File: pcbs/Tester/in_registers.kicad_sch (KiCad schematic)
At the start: 11 parts, among them U401 74HC165, U402 74HC165, U403 74HC165

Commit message: Lots of rethinking
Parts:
- added J401: Conn_02x20_Odd_Even, Connector_PinHeader_2.54mm:PinHeader_2x20_P2.54mm_Vertical, symbol Connector_Generic:Conn_02x20_Odd_Even
- added R409, R410, R411, R412, R413, R414, R415, R416, R417, R418, R419, R420, R421, R422, R423, R424, R425, R426, R427, R428, R429, R430, R431, R432, R433, R434, R435, R436, R437, R438, R439, R440: 1M, Resistor_SMD:R_0603_1608Metric, symbol Device:R
- added U403, U404: 74HC165, Package_SO:SOIC-16_3.9x9.9mm_P1.27mm, symbol 74xx:74HC165
- renumbered U403 to U405
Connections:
- net +5V: now also U403.16 (VCC), U404.16 (VCC)
- net GND: now also U405.10 (DS), R409.2, R410.2, R411.2, R412.2, R413.2, R414.2, R415.2, R416.2, R417.2, R418.2, R419.2, R420.2, R421.2, R422.2, R423.2, R424.2, R425.2, R426.2, R427.2, R428.2, R429.2, R430.2, R431.2, R432.2, R433.2, R434.2, R435.2, R436.2, R437.2, R438.2, R439.2, R440.2, U403.8 (GND), U404.8 (GND); no longer U401.10 (DS)
- net IN_{CLK}: now also U403.2 (CP), U404.2 (CP)
- net IN_{DATA}: now also U401.9 (Q7); no longer U405.9 (Q7)
- net ~{IN_{LOAD}}: now also U403.1 (~{PL}), U404.1 (~{PL})
- net ~{IN_{SELECT}}: now also U403.15 (~{CE}), U404.15 (~{CE})
- net at U402.10 (DS): now also U403.9 (Q7); no longer U401.9 (Q7)
- net at U402.9 (Q7): now also U401.10 (DS); no longer U405.10 (DS)
- net IN0: no longer names the net of U405.6 (D7)
- net IN0: no longer R401.1
- net IN1: no longer names the net of U405.5 (D6)
- net IN1: no longer R402.1
- net IN16 renamed In_{0}
- net In_{0}: now also R401.1, J401.1 (Pin_1)
- net IN17 renamed In_{1}
- net In_{1}: now also R402.1, J401.2 (Pin_2)
- net IN18 renamed In_{2}
- net In_{2}: now also R403.1, J401.3 (Pin_3)
- net IN19 renamed In_{3}
- net In_{3}: now also R404.1, J401.4 (Pin_4)
- net IN2: no longer names the net of U405.4 (D5)
- net IN2: no longer R403.1
- net IN20 renamed In_{4}
- net In_{4}: now also R405.1, J401.5 (Pin_5)
- net IN21 renamed In_{5}
- net In_{5}: now also R406.1, J401.6 (Pin_6)
- net IN22 renamed In_{6}
- net In_{6}: now also R407.1, J401.7 (Pin_7)
- net IN23 renamed In_{7}
- net In_{7}: now also R408.1, J401.8 (Pin_8)
- net IN3: no longer names the net of U405.3 (D4)
- net IN3: no longer R404.1
- net IN4: no longer names the net of U405.14 (D3)
- net IN4: no longer R405.1
- net IN5: no longer names the net of U405.13 (D2)
- net IN5: no longer R406.1
- net IN6: no longer names the net of U405.12 (D1)
- net IN6: no longer R407.1
- net IN7: no longer names the net of U405.11 (D0)
- net IN7: no longer R408.1
- new net: U404.10 (DS), U405.9 (Q7)
- new net: U403.10 (DS), U404.9 (Q7)
- new net In_{10}: J401.11 (Pin_11), R411.1
- new net In_{11}: J401.12 (Pin_12), R412.1
- new net In_{12}: J401.13 (Pin_13), R413.1
- new net In_{13}: J401.14 (Pin_14), R414.1
- new net In_{14}: J401.15 (Pin_15), R415.1
- new net In_{15}: J401.16 (Pin_16), R416.1
- new net In_{16}: J401.17 (Pin_17), R417.1
- new net In_{17}: J401.18 (Pin_18), R418.1
- new net In_{18}: J401.19 (Pin_19), R419.1
- new net In_{19}: J401.20 (Pin_20), R420.1
- new net In_{20}: J401.21 (Pin_21), R421.1
- new net In_{21}: J401.22 (Pin_22), R422.1
- new net In_{22}: J401.23 (Pin_23), R423.1
- new net In_{23}: J401.24 (Pin_24), R424.1
- new net In_{24}: J401.25 (Pin_25), R425.1
- new net In_{25}: J401.26 (Pin_26), R426.1
- new net In_{26}: J401.27 (Pin_27), R427.1
- new net In_{27}: J401.28 (Pin_28), R428.1
- new net In_{28}: J401.29 (Pin_29), R429.1
- new net In_{29}: J401.30 (Pin_30), R430.1
- new net In_{30}: J401.31 (Pin_31), R431.1
- new net In_{31}: J401.32 (Pin_32), R432.1
- new net In_{32}: J401.33 (Pin_33), R433.1
- new net In_{33}: J401.34 (Pin_34), R434.1
- new net In_{34}: J401.35 (Pin_35), R435.1
- new net In_{35}: J401.36 (Pin_36), R436.1
- new net In_{36}: J401.37 (Pin_37), R437.1
- new net In_{37}: J401.38 (Pin_38), R438.1
- new net In_{38}: J401.39 (Pin_39), R439.1
- new net In_{39}: J401.40 (Pin_40), R440.1
- new net In_{8}: J401.9 (Pin_9), R409.1
- new net In_{9}: J401.10 (Pin_10), R410.1
- no-connect marks 3 -> 5
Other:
- moved on the sheet: R401, R402, R403, R404, R405, R406, R407, R408, U401, U402, U405

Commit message: Thinking about the input side
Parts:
- added C401, C402, C403, C404, C405: 100n, Capacitor_SMD:C_0603_1608Metric, symbol Device:C
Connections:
- net +5V: now also C401.2, C402.2, C403.2, C404.2, C405.2
- net GND: now also C401.1, C402.1, C403.1, C404.1, C405.1

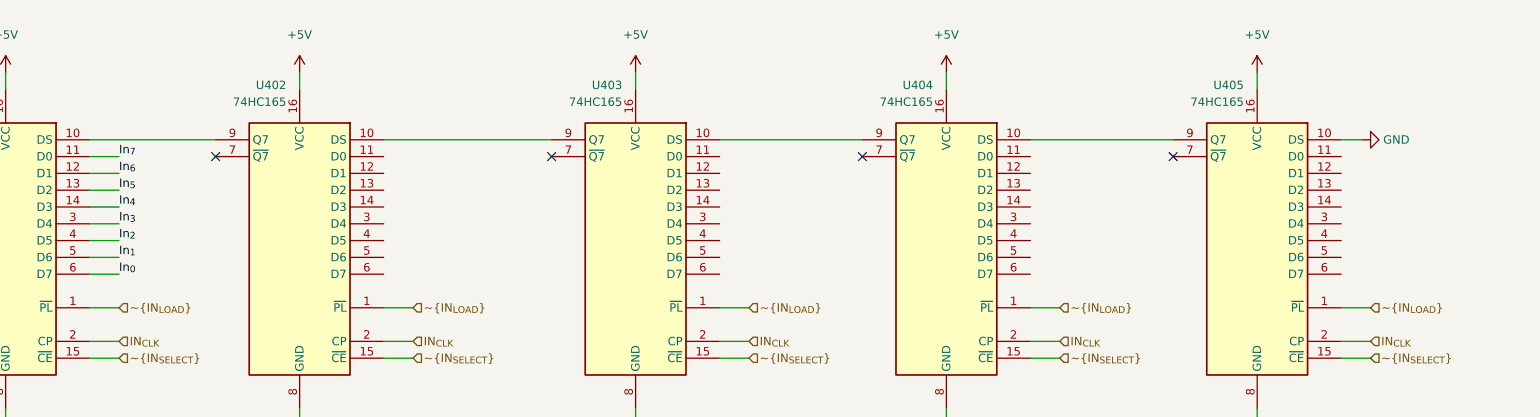
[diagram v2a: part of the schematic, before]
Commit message: Shift register routing
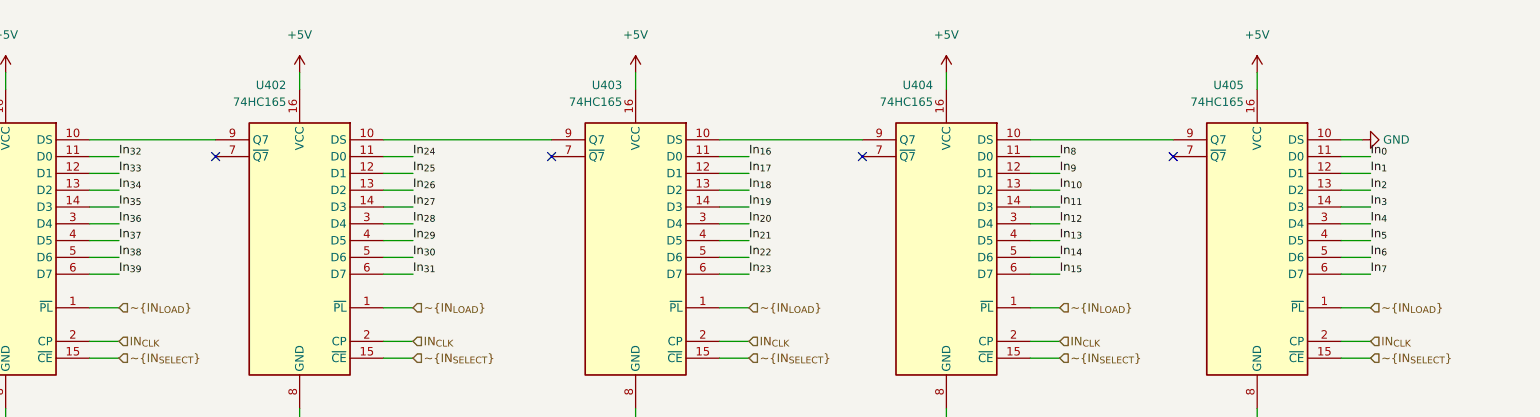
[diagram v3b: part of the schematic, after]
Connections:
- net In_{0}: now also U405.11 (D0); no longer U401.6 (D7)
- net In_{10}: now also U404.13 (D2)
- net In_{11}: now also U404.14 (D3)
- net In_{12}: now also U404.3 (D4)
- net In_{13}: now also U404.4 (D5)
- net In_{14}: now also U404.5 (D6)
- net In_{15}: now also U404.6 (D7)
- net In_{16}: now also U403.11 (D0)
- net In_{17}: now also U403.12 (D1)
- net In_{18}: now also U403.13 (D2)
- net In_{19}: now also U403.14 (D3)
- net In_{1}: now also U405.12 (D1); no longer U401.5 (D6)
- net In_{20}: now also U403.3 (D4)
- net In_{21}: now also U403.4 (D5)
- net In_{22}: now also U403.5 (D6)
- net In_{23}: now also U403.6 (D7)
- net In_{24}: now also U402.11 (D0)
- net In_{25}: now also U402.12 (D1)
- net In_{26}: now also U402.13 (D2)
- net In_{27}: now also U402.14 (D3)
- net In_{28}: now also U402.3 (D4)
- net In_{29}: now also U402.4 (D5)
- net In_{2}: now also U405.13 (D2); no longer U401.4 (D5)
- net In_{30}: now also U402.5 (D6)
- net In_{31}: now also U402.6 (D7)
- net In_{32}: now also U401.11 (D0)
- net In_{33}: now also U401.12 (D1)
- net In_{34}: now also U401.13 (D2)
- net In_{35}: now also U401.14 (D3)
- net In_{36}: now also U401.3 (D4)
- net In_{37}: now also U401.4 (D5)
- net In_{38}: now also U401.5 (D6)
- net In_{39}: now also U401.6 (D7)
- net In_{3}: now also U405.14 (D3); no longer U401.3 (D4)
- net In_{4}: now also U405.3 (D4); no longer U401.14 (D3)
- net In_{5}: now also U405.4 (D5); no longer U401.13 (D2)
- net In_{6}: now also U405.5 (D6); no longer U401.12 (D1)
- net In_{7}: now also U405.6 (D7); no longer U401.11 (D0)
- net In_{8}: now also U404.11 (D0)
- net In_{9}: now also U404.12 (D1)
